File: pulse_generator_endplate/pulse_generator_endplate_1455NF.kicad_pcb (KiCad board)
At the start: 2 copper layers, 103 x 53 mm, 1 part, among them J1 Conn_01x01_Pin

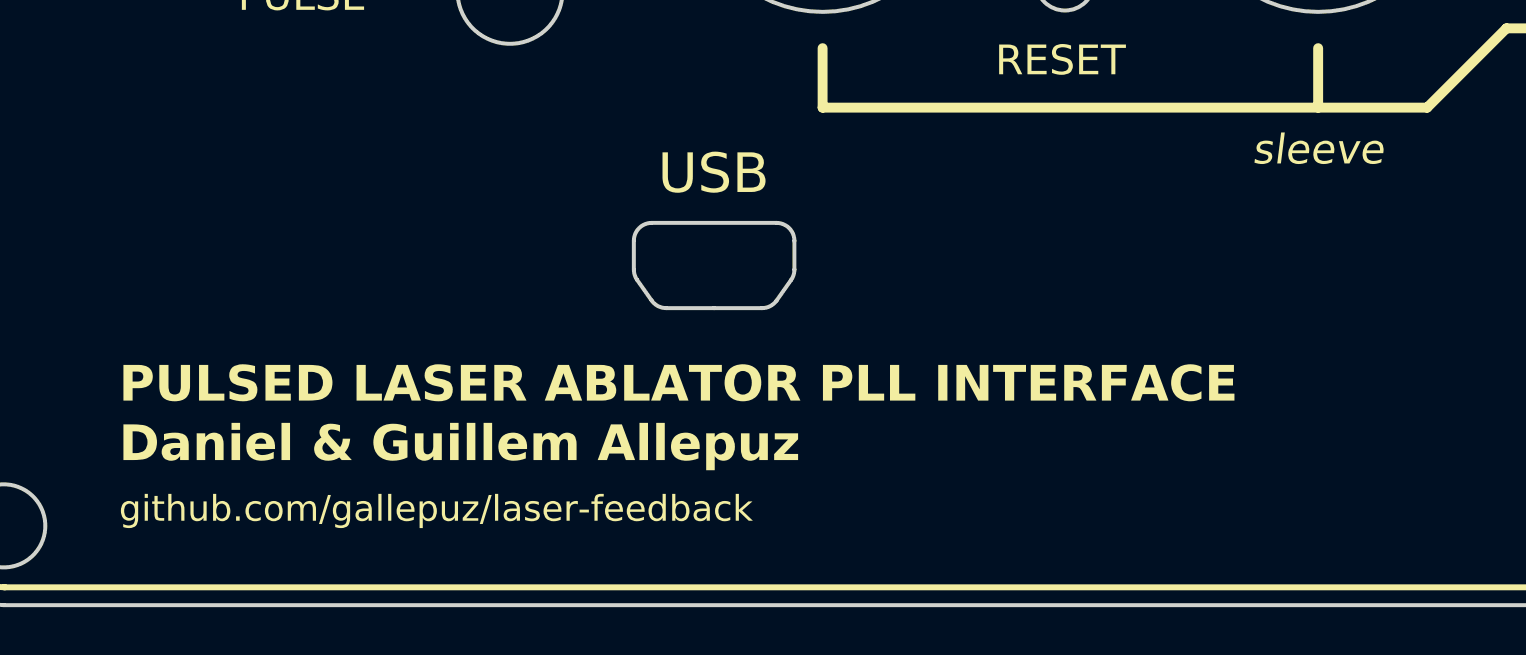
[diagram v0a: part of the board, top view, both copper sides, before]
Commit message: rearrange diode clamp section
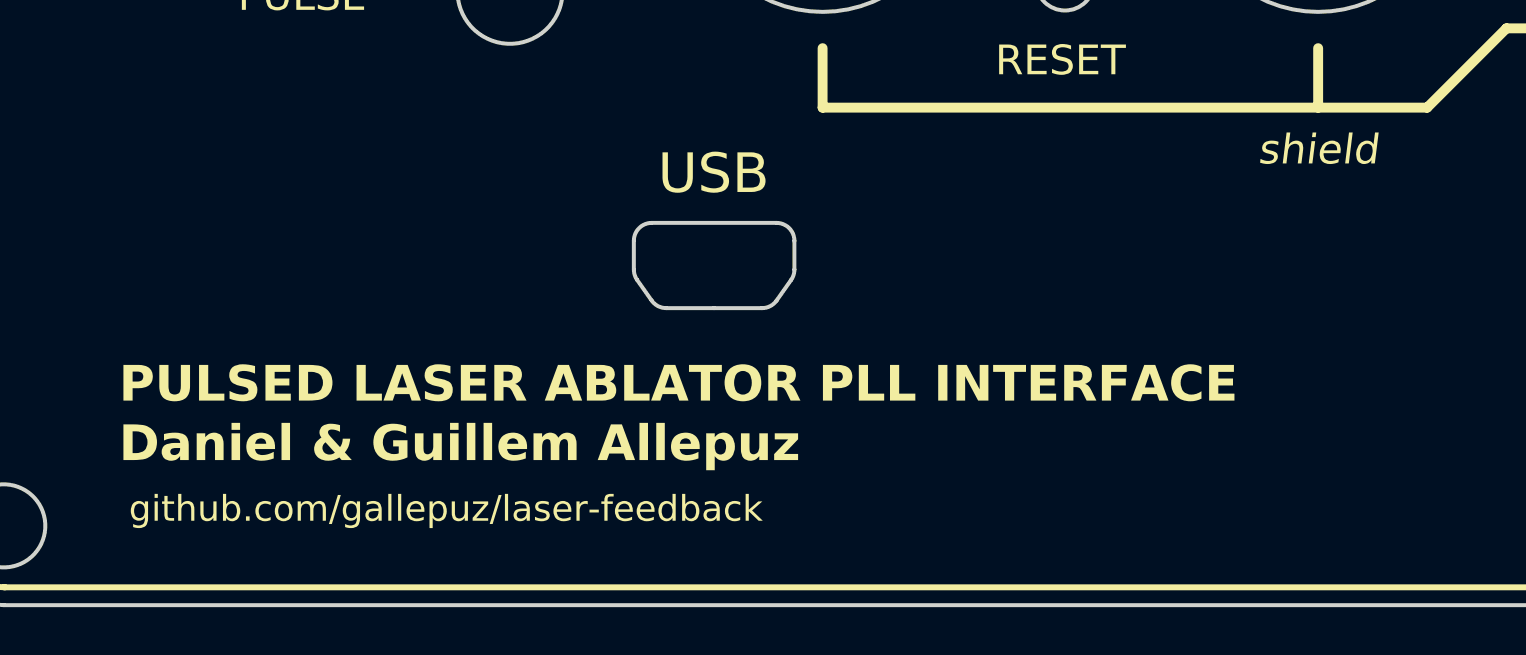
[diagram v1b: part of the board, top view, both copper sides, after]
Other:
- board text added: "shield"
- board text removed: "sleeve"
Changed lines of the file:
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@@
     (effects (font (size 1.5 1.5) (thickness 0.3)) (justify bottom))
   )
-  (gr_text "sleeve" (at 161.5 95) (layer "F.SilkS")
+  (gr_text "shield" (at 161.5 95) (layer "F.SilkS")
     (effects (font (size 1.5 1.5) (thickness 0.3) italic) (justify bottom))
   )
-  (gr_text "github.com/gallepuz/laser-feedback" (at 101 113) (layer "F.SilkS" knockout)
+  (gr_text "github.com/gallepuz/laser-feedback" (at 101.5 113) (layer "F.SilkS" knockout)
     (effects (font (size 1.3 1.3) (thickness 0.2)) (justify left bottom))
   )

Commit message: Please enter the commit message for your changes. Lines starting
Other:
- board text added: "WayWayWay"
